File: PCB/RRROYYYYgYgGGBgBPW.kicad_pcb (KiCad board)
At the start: 2 copper layers, 24 x 24 mm, 36 parts, among them K1 CONN_6, SW1 SPST, SW2 SW_PUSH, SW3 SW_PUSH, U1 ATTINY85-M, U2 AAT1217-3.3, U3 74HC595, U4 74HC595

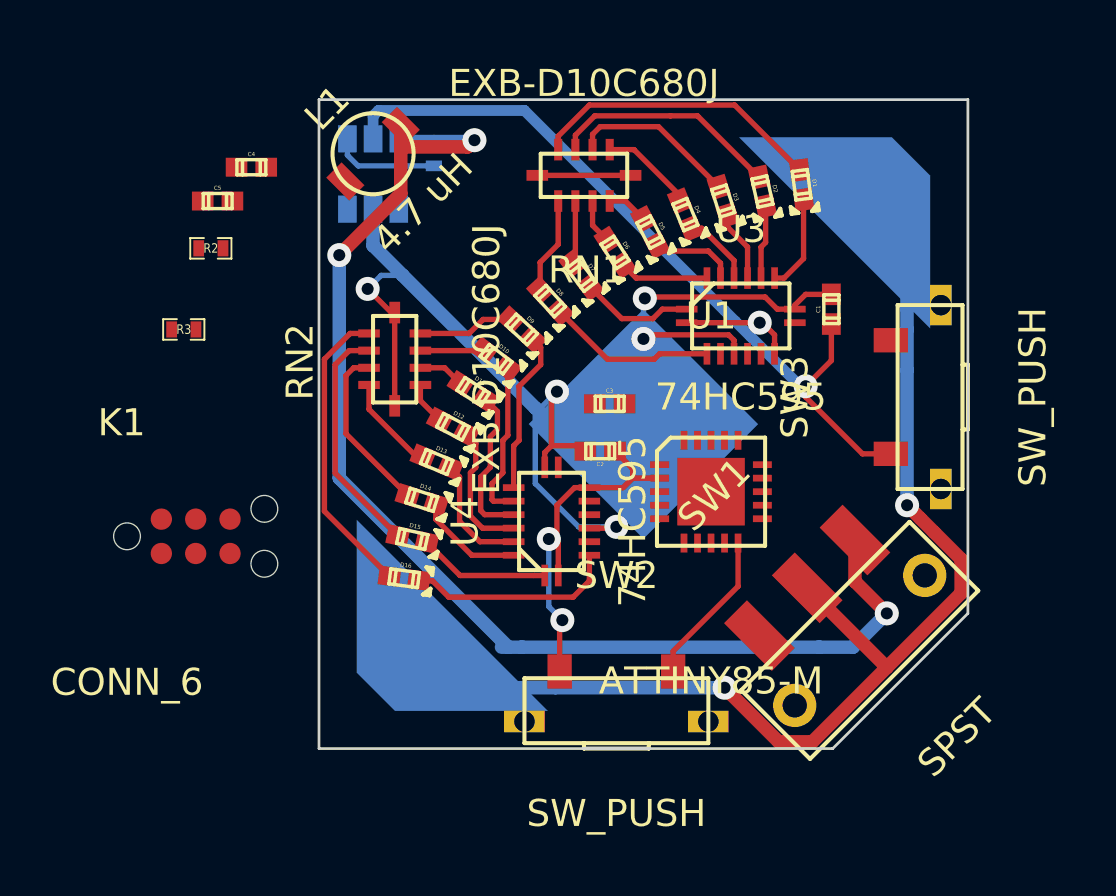
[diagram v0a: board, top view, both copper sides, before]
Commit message: changed the file names to reflect addition of pink and white LEDs. finished routing, beefed up power rails, rounded corners. changed processor footprint to TSSOP. still needs a thorough review...
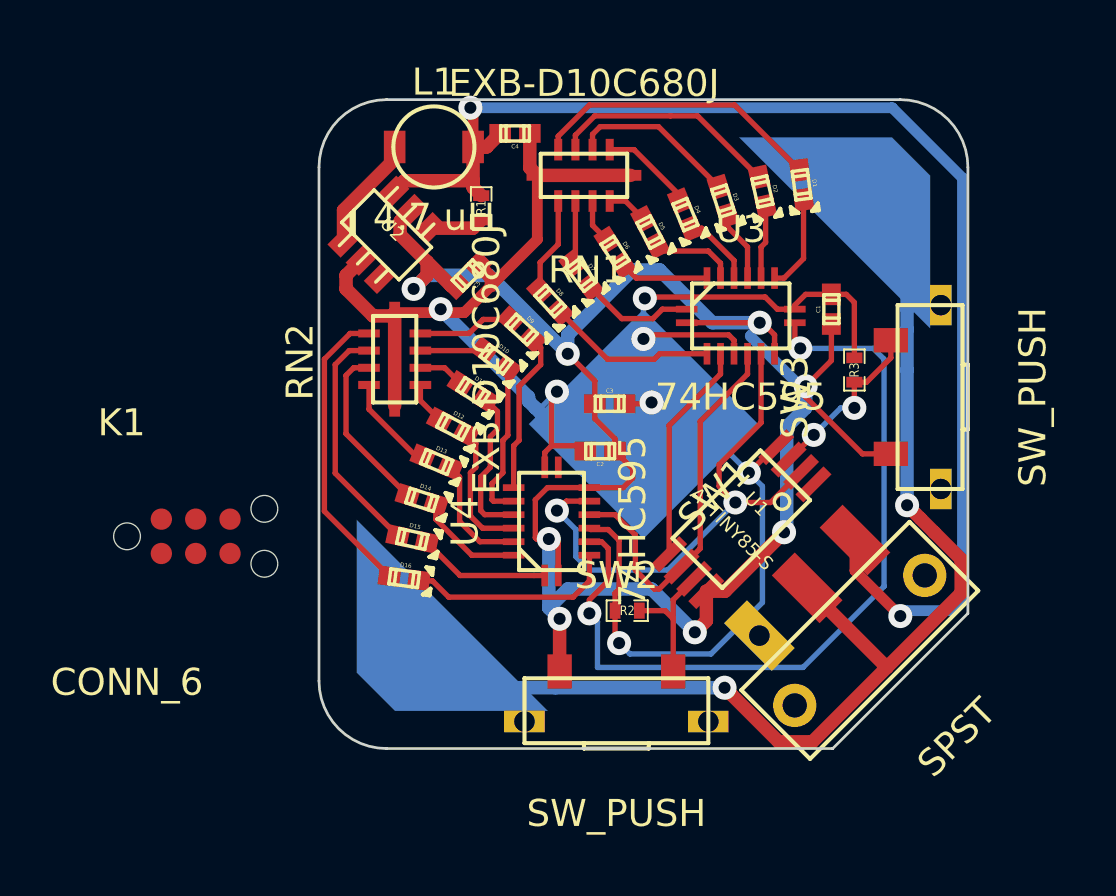
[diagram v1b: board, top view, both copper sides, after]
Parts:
- R1, U2: moved to F.Cu
- U1: value ATTINY85-M -> ATTINY85-S; footprint QFN20 -> tssop-8
- moved R3 24.8 mm to (119.8, 34.0), turned to 90 degrees
- moved R2 20.4 mm to (111.4, 42.9), turned to 180 degrees
- moved C4 9.83 mm to (107.2, 25.2), turned to 180 degrees
- moved C5 9.65 mm to (105.5, 30.5), turned to 225 degrees
- moved R1 2.66 mm to (106.0, 28.0)
- moved U2 2.30 mm to (102.5, 29.0), turned to 315 degrees
- moved L1 2.26 mm to (104.2, 25.8), turned to 0 degrees
- moved U1 0.22 mm to (114.7, 38.6), turned to 135 degrees
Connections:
- K1 pad 1: VCC -> (no net)
- K1 pad 2: GND -> (no net)
- K1 pad 3: N-000001 (its old number) -> (no net)
- K1 pad 4: N-0000033 (its old number) -> (no net)
- K1 pad 5: N-000003 (its old number) -> (no net)
- K1 pad 6: N-000002 (its old number) -> (no net)
- R2 pad 1: N-000003 (its old number) -> N-0000022
- R3 pad 1: N-000002 (its old number) -> N-0000025
- SW2 pad 2: N-000003 (its old number) -> N-0000022
- SW3 pad 2: N-000002 (its old number) -> N-0000025
- U1 pad 3: (no net) -> N-0000025
- U1 pad 4: (no net) -> GND
- U1 pad 7: (no net) -> N-0000022
- U1 pad 8: GND -> VCC
- U3 pad 11: N-0000035 (its old number) -> N-0000024
- U3 pad 12: N-0000033 (its old number) -> N-0000028
- U4 pad 11: N-0000035 (its old number) -> N-0000024
- U4 pad 12: N-0000033 (its old number) -> N-0000028
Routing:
- net N-0000036: track 0.00 -> 30.2 mm, vias 0 -> 2
- net GND: track 56.2 -> 83.7 mm, vias 5 -> 7
- net VCC: track 46.8 -> 72.6 mm, vias 4 -> 8
- net N-0000024: track 0.00 -> 19.8 mm, vias 0 -> 2
- net N-0000028: track 0.00 -> 14.5 mm
- net N-0000023: track 0.00 -> 8.20 mm
- net N-0000025: track 0.00 -> 6.55 mm, vias 0 -> 2
- net N-000003 (its old number): track 5.74 -> 0.00 mm
- net N-0000022: track 0.00 -> 5.12 mm
- net N-000004: track 0.00 -> 4.28 mm
- net N-000001: track 46.5 -> 48.6 mm, vias 3 -> 2
- net N-000003: track 3.97 -> 2.03 mm
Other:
- outline, holes or cut-outs redrawn

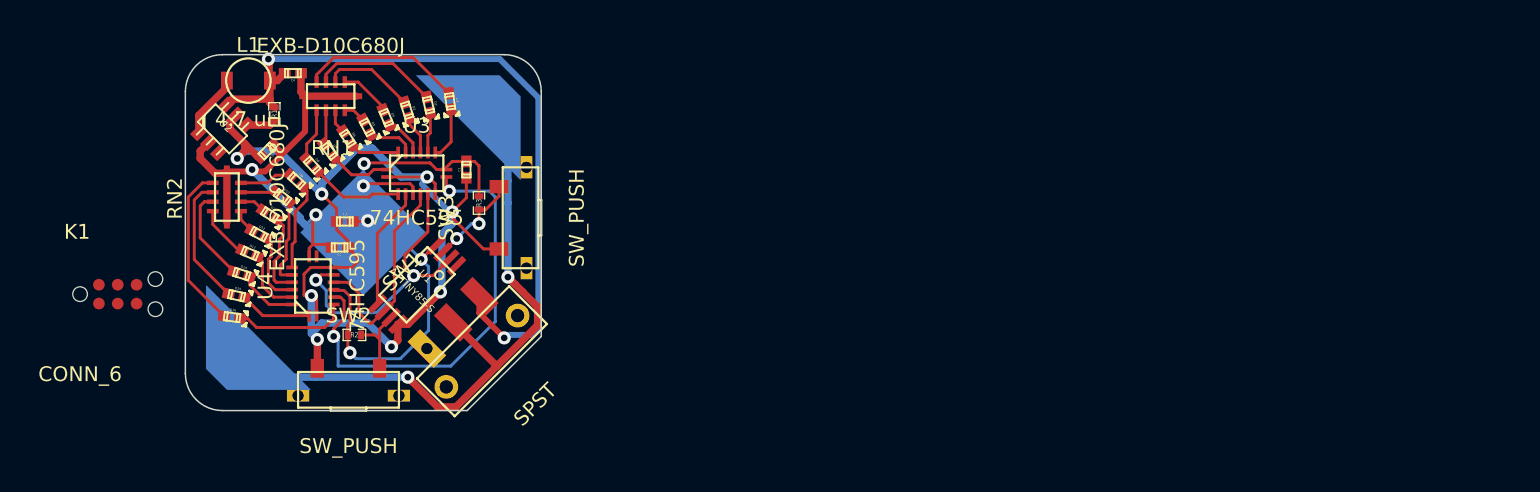
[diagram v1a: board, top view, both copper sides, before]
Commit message: changed from 3.3vdc boost converter + 2032 coin cell to usb plug power. added silkscreen, re-routed, etc. resistor network value still TBD, i'm afraid (it worked at 3.3vdc, but might not here...)
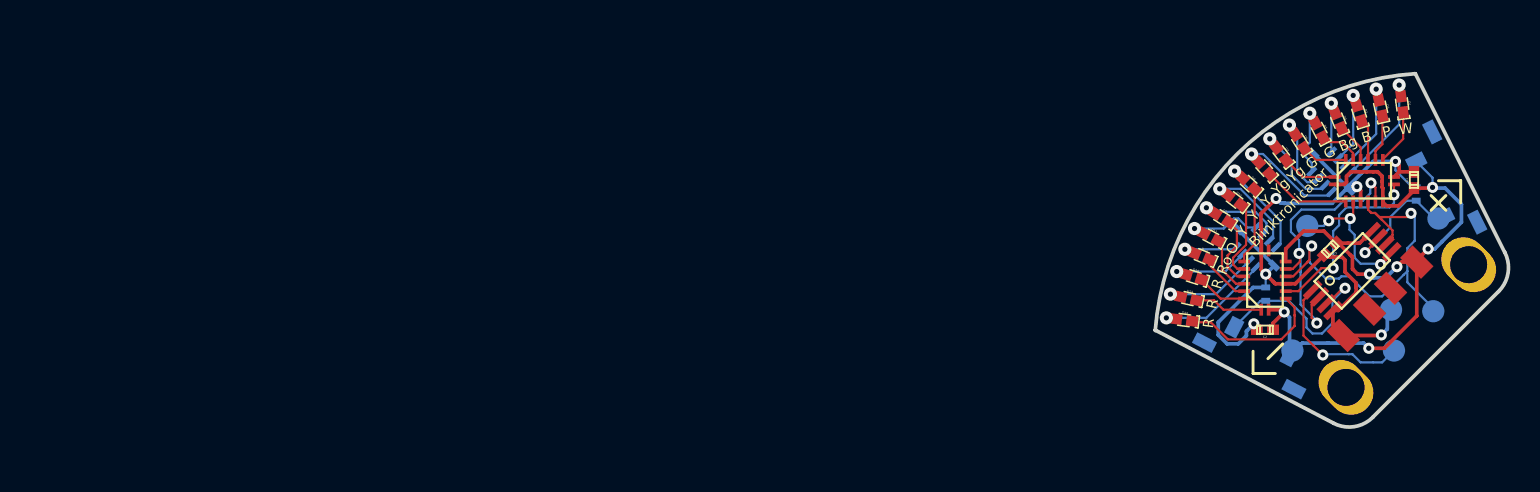
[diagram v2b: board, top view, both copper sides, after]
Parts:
- removed BT1: BATTERY, CR2032_smd
- removed C4, C5: 4.7 uF, c_0402
- removed K1: CONN_6, tag-connect-TC2030-IDC-NL
- removed L1: 4.7 uH, VLF3012A
- removed R1: 1M, SM0402
- removed SW1: SPST, JS102011SAQN
- removed U2: AAT1217-3.3, tsot-6
- added CONN1: USB_PLUG, USBplug, F.Cu at (182.4, 42.3)
- added P1: VCC, PAD_1-5mm, B.Cu at (174.7, 44.0)
- added P2: GND, PAD_1-5mm, B.Cu at (181.3, 41.2)
- added P3: RST, PAD_1-5mm, B.Cu at (181.5, 44.0)
- added P4: SCK, PAD_1-5mm, B.Cu at (184.5, 35.0)
- added P5: MISO, PAD_1-5mm, B.Cu at (184.2, 41.3)
- added P6: MOSI, PAD_1-5mm, B.Cu at (175.7, 35.5)
- R2, R3, RN1, RN2, SW2, SW3: moved to B.Cu
- moved SW2 74.9 mm to (184.7, 32.7), turned to 296.5 degrees
- moved R2 72.2 mm to (183.0, 33.4), turned to 90 degrees
- moved RN2 69.5 mm to (172.2, 37.0), turned to 315 degrees
- moved RN1 67.7 mm to (177.3, 31.9), turned to 315 degrees
- moved C3 66.5 mm to (177.2, 37.1), turned to 225 degrees
- moved U1 64.9 mm to (179.6, 39.5), turned to 315 degrees
- moved U4 64.2 mm to (172.8, 39.2)
- moved D1 64.2 mm to (182.1, 27.4)
- moved D13 64.2 mm to (168.6, 37.6)
- moved D10 64.2 mm to (170.8, 33.8)
- moved D11 64.2 mm to (169.9, 35.0)
- moved D12 64.2 mm to (169.2, 36.3)
- moved D14 64.2 mm to (168.0, 39.0)
- moved D15 64.2 mm to (167.7, 40.5)
- moved D3 64.2 mm to (179.2, 27.9)
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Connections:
- U1 pad 1: (no net) -> N-0000018
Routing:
- net N-000001 (its old number): track 48.6 -> 0.00 mm, vias 2 -> 0
- net N-000002 (its old number): track 44.1 -> 0.00 mm, vias 2 -> 0
- net GND: track 83.7 -> 56.9 mm, vias 7 -> 6
- net VCC: track 72.6 -> 54.3 mm, vias 8 -> 6
- net N-000004: track 30.2 -> 12.9 mm
- net N-0000017: track 14.5 -> 27.1 mm, vias 0 -> 2
- net N-0000018: track 0.00 -> 10.7 mm, vias 0 -> 1
- net N-0000013: track 6.55 -> 13.3 mm, vias 2 -> 1
- net N-0000041: track 1.66 -> 6.01 mm, vias 0 -> 1
- net N-0000037: track 1.73 -> 6.08 mm, vias 0 -> 1
- net N-000004 (its old number): track 4.28 -> 0.00 mm
- net N-0000038: track 2.37 -> 6.63 mm, vias 0 -> 1
- net N-0000042: track 2.36 -> 6.58 mm, vias 0 -> 1
- net N-0000014: track 5.12 -> 8.98 mm, vias 0 -> 1
- net N-0000033: track 1.59 -> 5.42 mm, vias 0 -> 1
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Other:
- board size 24 x 24 mm -> 23.8 x 23.8 mm
- net class Default: clearance 0.18 -> 0.225; trace_width 0.2 -> 0.15; via_dia 0.889 -> 0.75; via_drill 0.635 -> 0.35
- rule trace_clearance: 0.18 -> 0.225
- rule trace_min: 0.2 -> 0.15
- rule via_min_drill: 0.508 -> 0.35
- rule via_min_size: 0.889 -> 0.75
- board text added: "B"
- board text added: "Bg"
- board text added: "Blinktronicator"
- board text added: "G"
- board text added: "O"
- board text added: "P"
- board text added: "R"
- board text added: "Ro"
- board text added: "W"
- board text added: "Y"
- board text added: "Yg"
- board text added: "Zach Fredin December 2015"

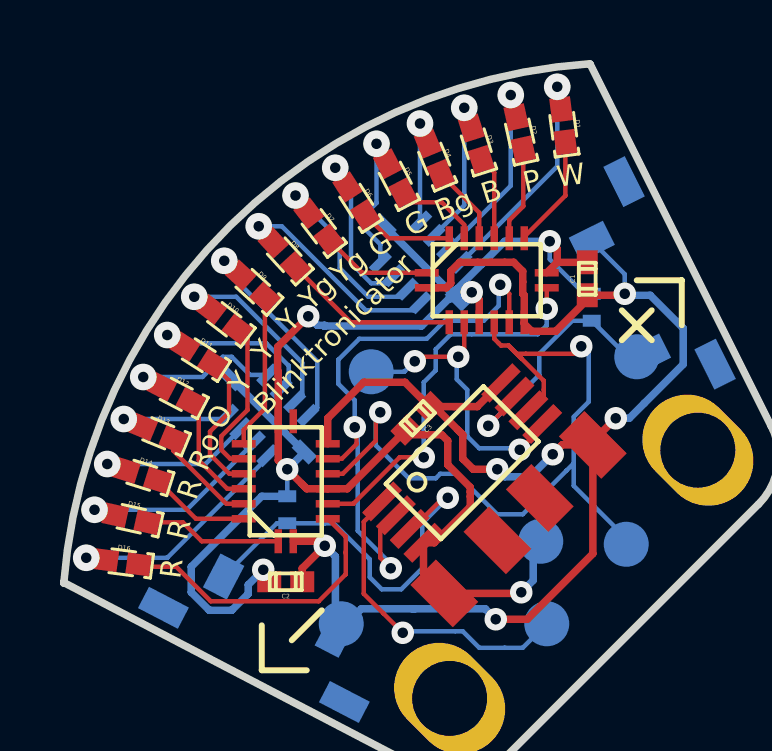
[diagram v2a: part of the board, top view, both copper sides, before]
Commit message: realized the resistor networks were sized for 3.3vdc power; moving to 5vdc power means the shorter wavelength stuff needs a different value. bodged in a quartet of 0402 resistors, mounted on the back. symmetry is pretty much horrible now.
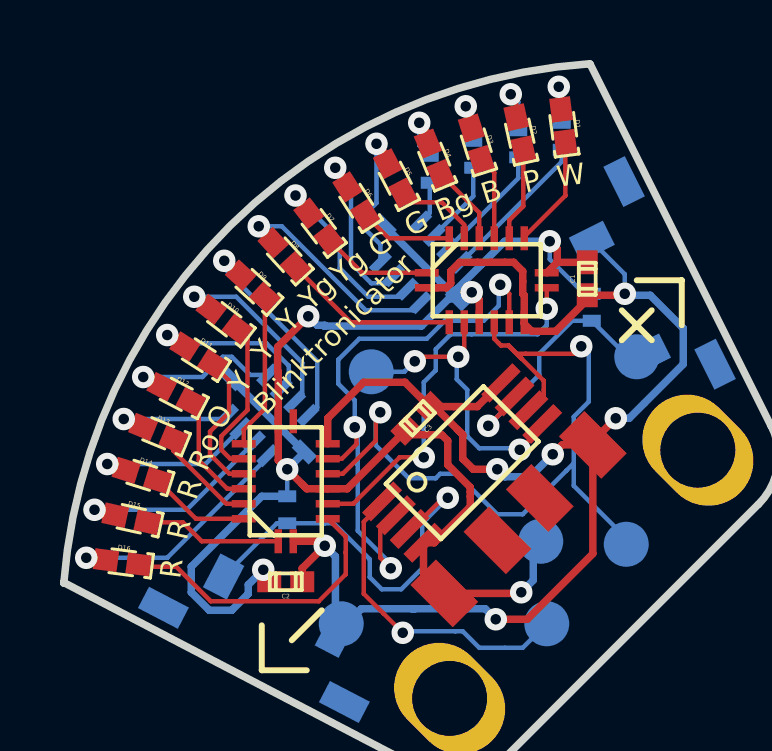
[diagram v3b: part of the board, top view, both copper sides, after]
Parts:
- added R1: R, SM0402, B.Cu at (177.6, 28.8)
- added R4: R, SM0402, B.Cu at (180.6, 27.9)
- added R5: R, SM0402, B.Cu at (179.1, 28.3)
- added R6: R, SM0402, B.Cu at (182.0, 27.7)
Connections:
- D1 pad 2: N-0000028 (its old number) -> N-0000011
- D2 pad 2: N-000007 -> N-0000010
- D3 pad 2: N-000006 -> N-000008
- RN1 pad 10: N-000005 -> N-000006
- RN1 pad 7: N-0000028 (its old number) -> N-0000020
- RN1 pad 8: N-000007 -> N-000009
- RN1 pad 9: N-000006 -> N-000007
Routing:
- net N-0000028 (its old number): track 7.97 -> 0.00 mm, vias 1 -> 0
- net N-0000020: track 0.00 -> 5.14 mm
- net N-000009: track 0.00 -> 4.03 mm
- net N-000007: track 6.81 -> 2.79 mm, vias 1 -> 0
- net N-000006: track 5.43 -> 1.43 mm, vias 1 -> 0
- net N-000008: track 0.00 -> 2.32 mm, vias 0 -> 1
- net N-0000011: track 0.00 -> 2.28 mm, vias 0 -> 1
- net N-0000010: track 0.00 -> 2.14 mm, vias 0 -> 1
- net N-000005: track 4.06 -> 2.06 mm
